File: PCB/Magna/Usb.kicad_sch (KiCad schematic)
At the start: 54 parts, among them J401 USB_A, J402 USB_C_Receptacle_USB2.0, J403 USB_B, U401 SRV05-4, U402 USB3300-EZK, U403 SRV05-4

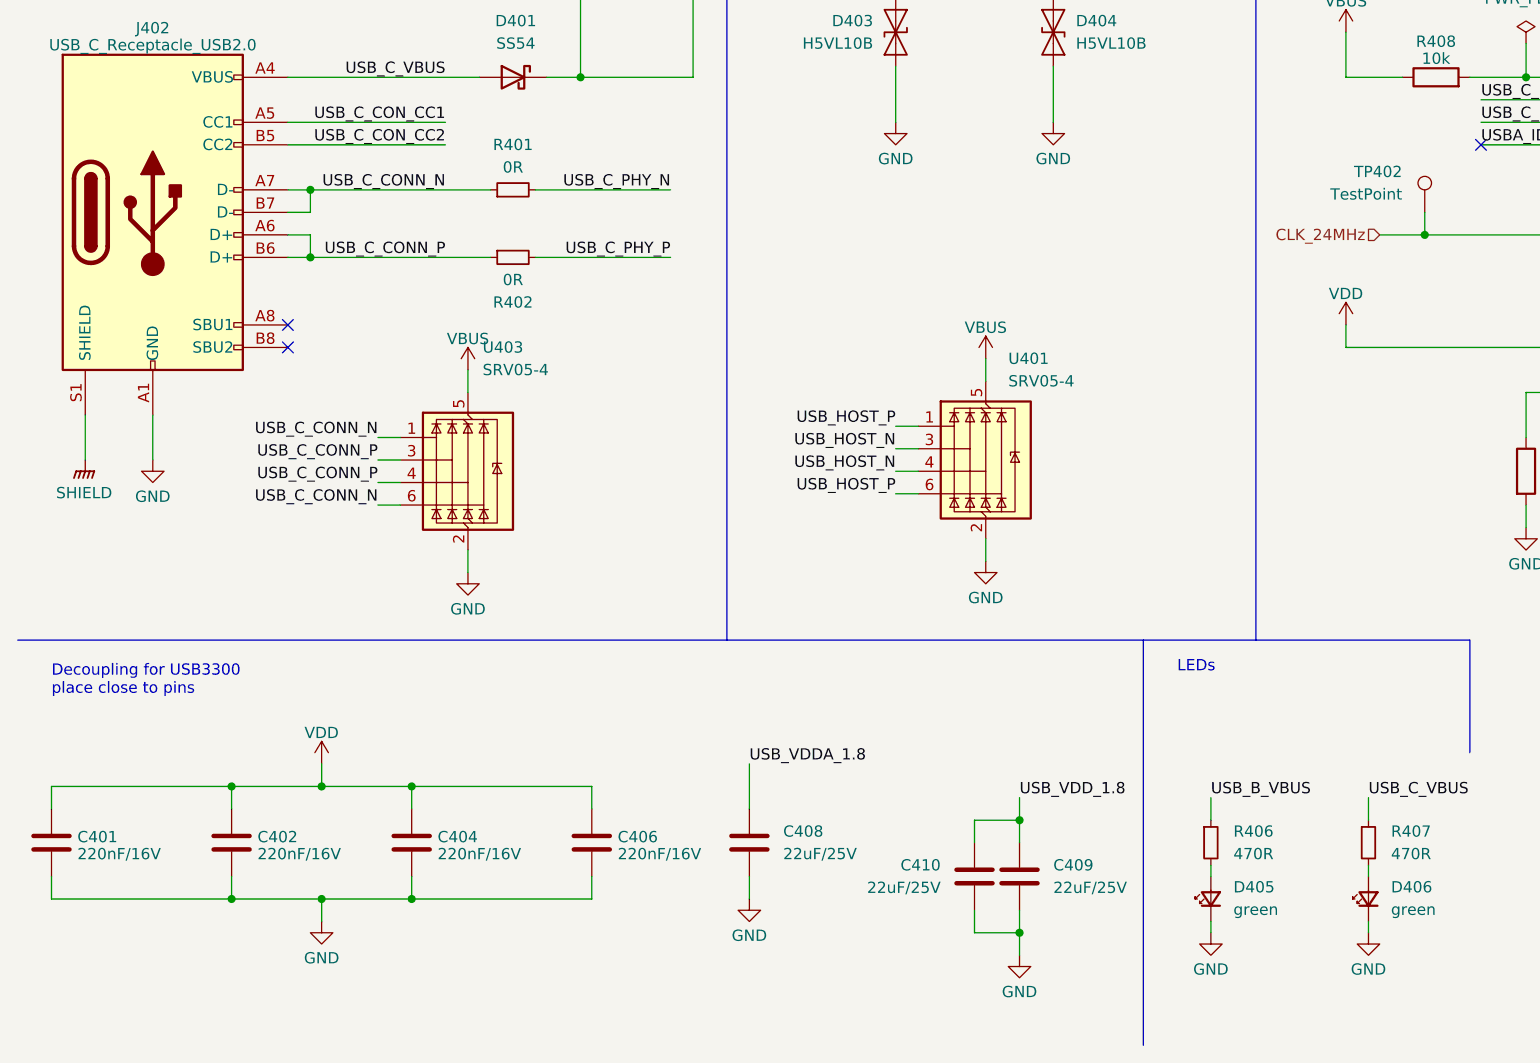
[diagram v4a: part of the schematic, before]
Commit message: Update schematics to Kicad 9
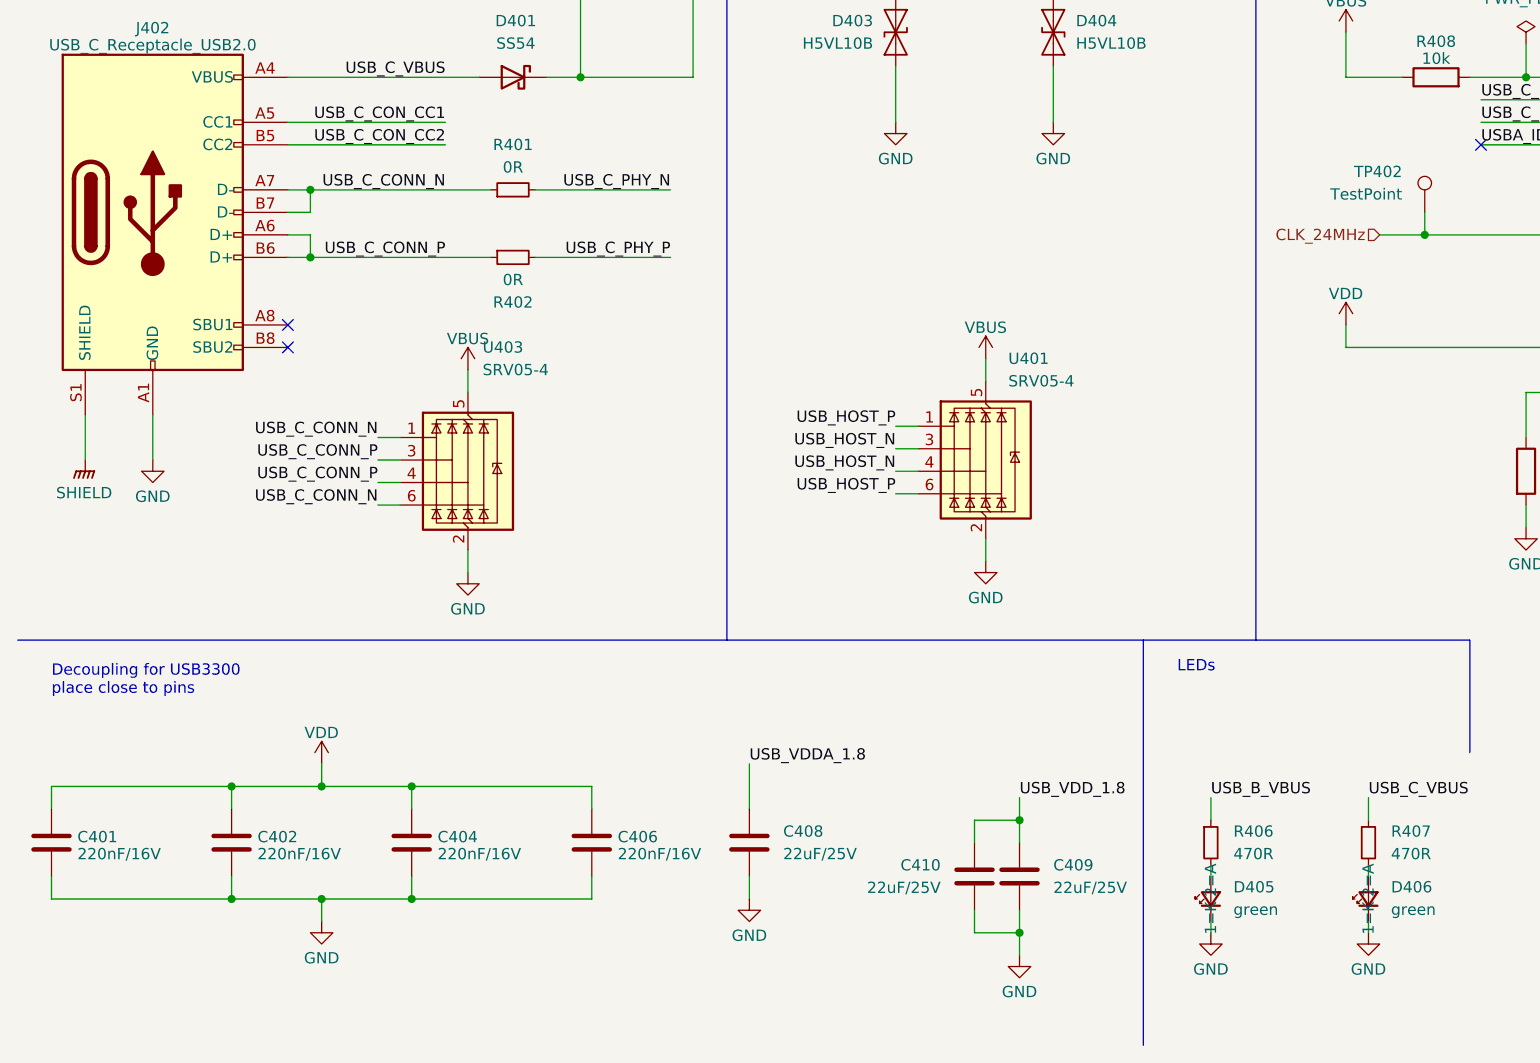
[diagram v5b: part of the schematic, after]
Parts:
- D403, D404: footprint Diode_SMD:D_0402_1005Metric -> Diode_SMD:D_SOD-923

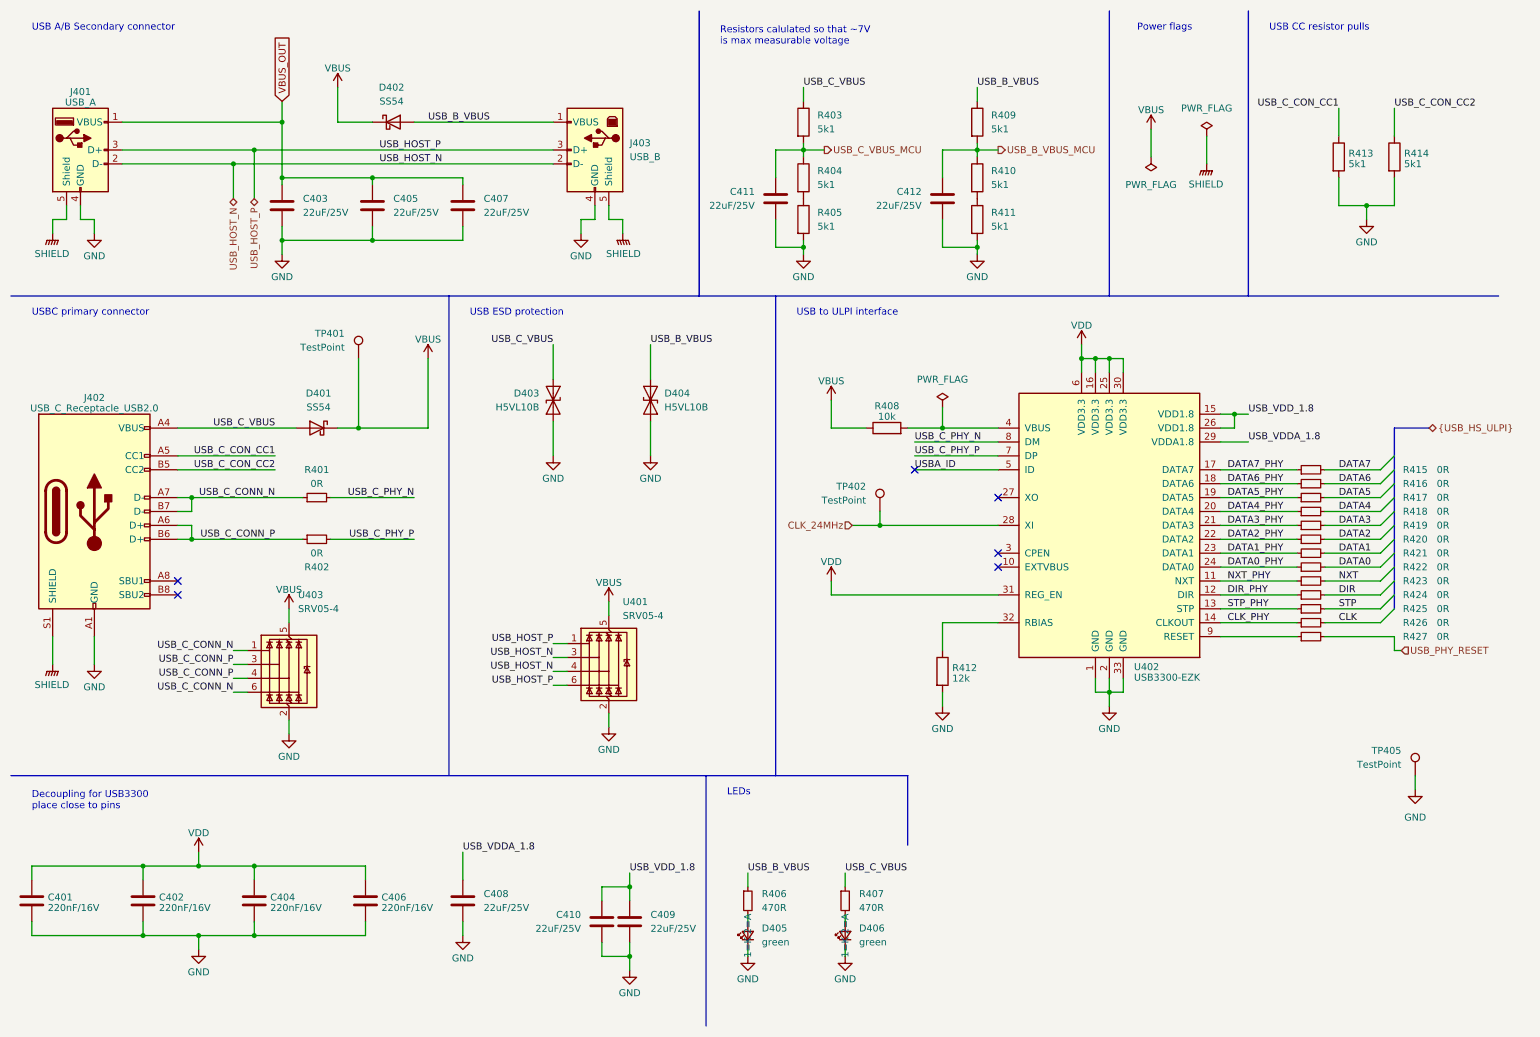
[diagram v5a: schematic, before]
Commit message: Update Mainboard PCB
* Added better power ORing
* Added DRC for length matching
* Changed out components for cheaper production
* Removed some optional circuits from BOM for first prototype
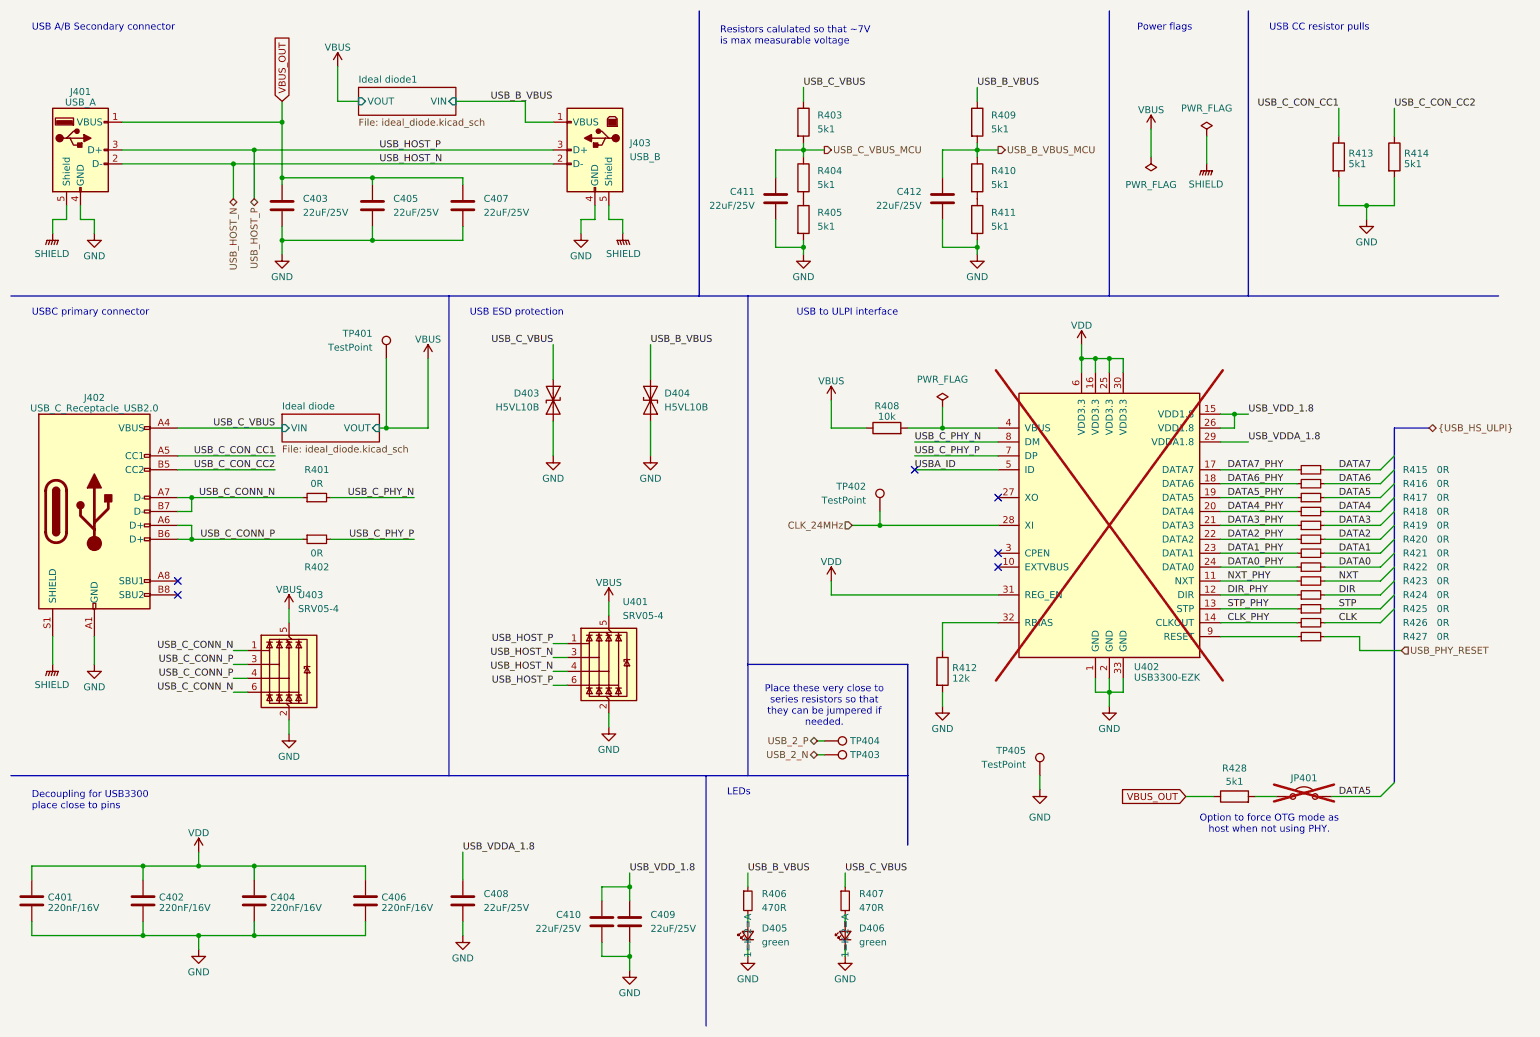
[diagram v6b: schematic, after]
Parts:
- removed D401, D402: SS54, Diode_SMD:D_SMA_Handsoldering, symbol Device:D_Schottky
- added JP401: Jumper_2_Open, TestPoint:TestPoint_2Pads_Pitch2.54mm_Drill0.8mm, symbol Jumper:Jumper_2_Open
- added R428: 5k1, Resistor_SMD:R_0805_2012Metric_Pad1.20x1.40mm_HandSolder, symbol Device:R
- added TP403, TP404: TestPoint, Connector_PinHeader_1.00mm:PinHeader_1x01_P1.00mm_Vertical, symbol Connector:TestPoint
- D403, D404: footprint Diode_SMD:D_SOD-923 -> Diode_SMD:D_SMB_Handsoldering; LCSC C7420372 -> C78395
- J401, J403, TP401, TP402, TP405: now left out of the parts list
- U402: now not fitted; now left out of the parts list
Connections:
- net DATA5: now also JP401.2 (B)
- net VBUS_OUT: now also R428.1
- new net: JP401.1 (A), R428.2
- new net USB_2_N: TP403.1
- new net USB_2_P: TP404.1
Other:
- added sheet Ideal diode (ideal_diode.kicad_sch)
- added sheet Ideal diode1 (ideal_diode.kicad_sch)
- note added: "Option to force OTG mode as host when not using PHY."
- note added: "Place these very close to series resistors so that they can be jumpered if needed."
- moved on the sheet: TP401, TP405
